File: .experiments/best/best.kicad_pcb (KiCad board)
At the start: 2 copper layers, 140 x 90 mm, 39 parts, among them J1 USB_C, J2 Output, J3 Debug, Q1 FS8205A, U1 USBLC6-2SC6, U2 BQ24072, U3 HY2113-KB5B, U4 MT3608, U5 AP2112K-3.3, U6 LN61CN3302MR-G

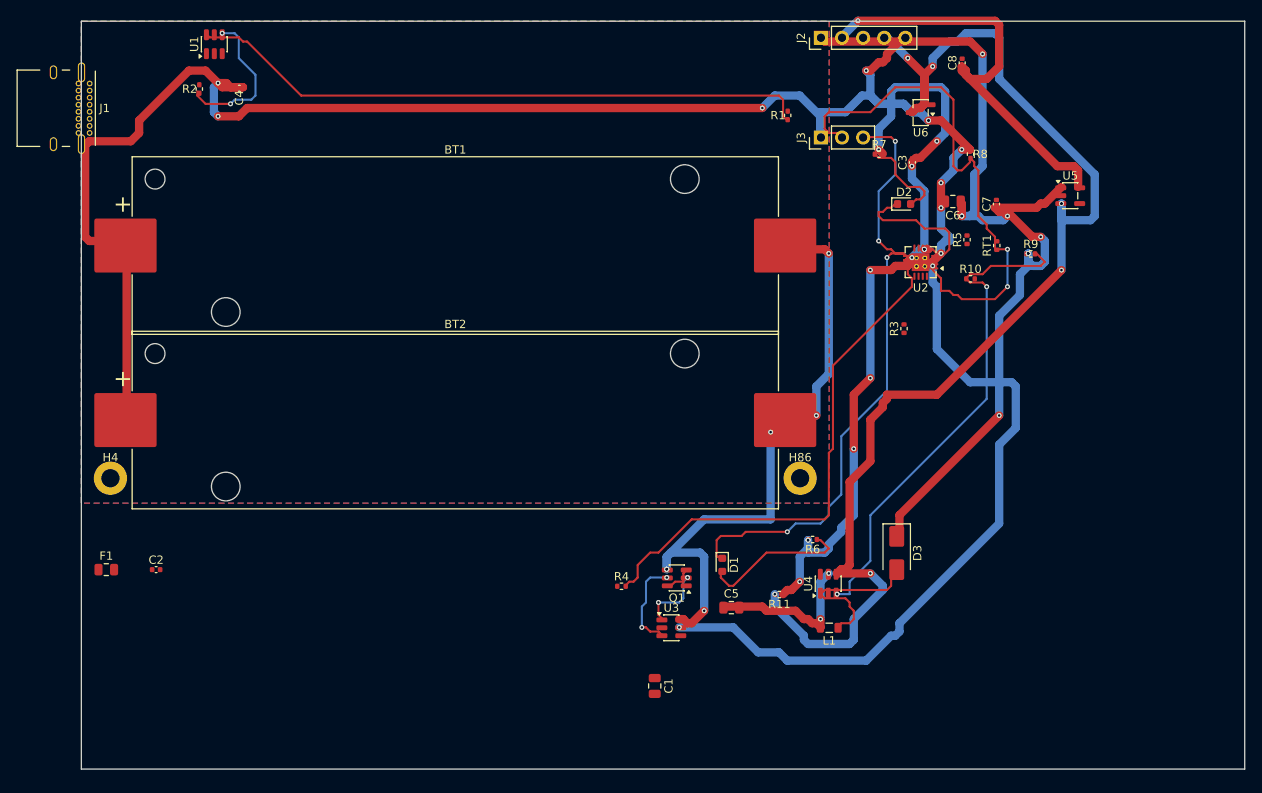
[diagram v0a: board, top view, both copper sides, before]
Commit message: 45-round experiment: best score 25.66, all nets routed (26/26)
Fixed A* performance by increasing max_search from 100k->500k to handle
high trace costs (100.0) without timing out. Kept high cost + coarse grid
(0.5mm) to prevent shorts while still routing efficiently.

Best config: edge_margin=5.7493mm, cooling_factor=0.9764, existing_trace_cost=200, max_rips=8

Co-Authored-By: Claude Opus 4.6 <noreply@anthropic.com>
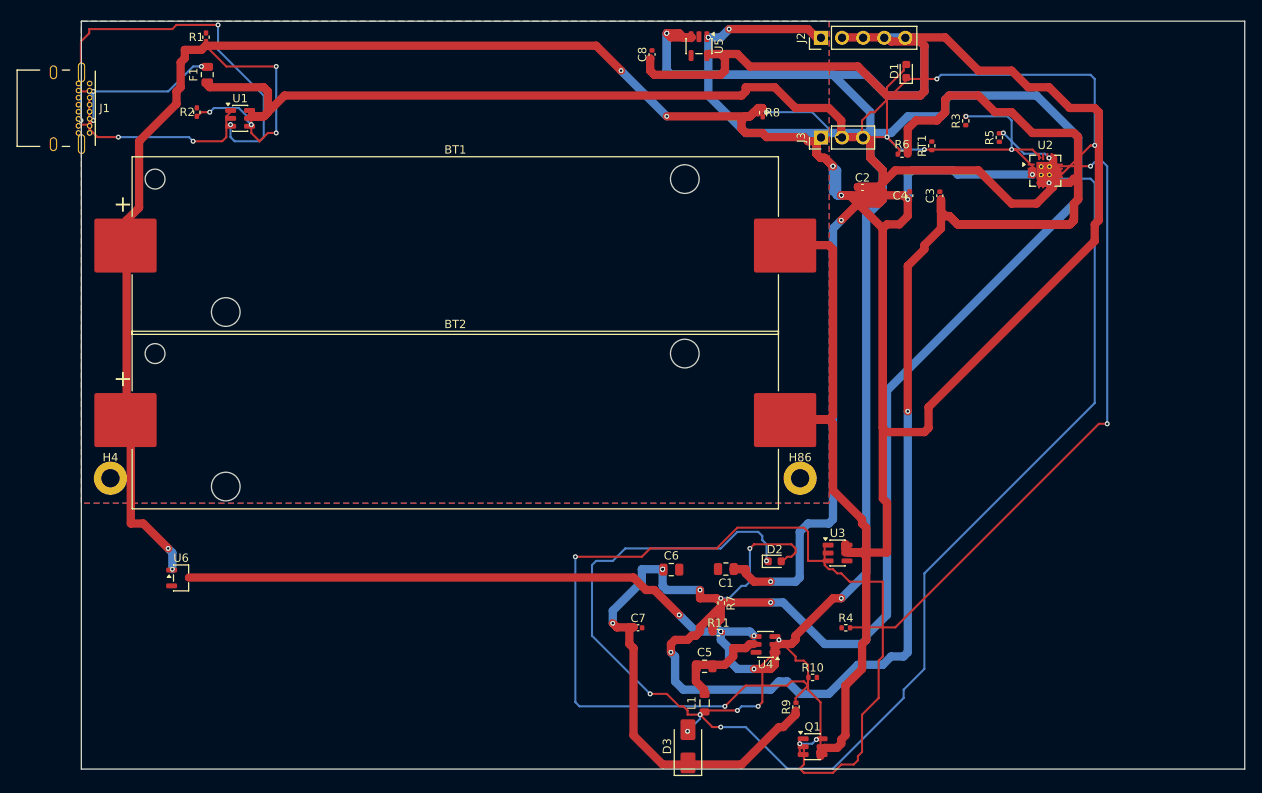
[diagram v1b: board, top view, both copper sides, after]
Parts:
- moved U6 105.2 mm to (12.0, 67.0), turned to 0 degrees
- moved C2 96.6 mm to (94.0, 20.0)
- moved C4 81.7 mm to (99.7, 21.0), turned to 90 degrees
- moved R1 70.6 mm to (15.0, 1.92)
- moved C7 66.8 mm to (67.0, 73.0), turned to 0 degrees
- moved D1 63.4 mm to (99.3, 6.00), turned to 90 degrees
- moved R9 61.4 mm to (86.0, 82.5), turned to 90 degrees
- moved F1 60.8 mm to (15.2, 6.43), turned to 90 degrees
- moved R7 57.3 mm to (77.0, 70.0), turned to -90 degrees
- moved C6 55.8 mm to (71.0, 66.0), turned to 0 degrees
- moved R10 51.6 mm to (88.0, 79.0)
- moved U5 48.2 mm to (74.3, 3.00), turned to -90 degrees
- moved R6 47.6 mm to (98.8, 16.0), turned to 0 degrees
- moved D2 45.7 mm to (83.4, 65.0)
- moved C8 37.3 mm to (68.7, 4.00)
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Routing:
- net /VBUS: track 0.00 -> 197.8 mm, vias 0 -> 2
- net Net-(D2-K): track 18.7 -> 159.5 mm, vias 0 -> 4
- net /5V: track 115.5 -> 224.6 mm, vias 8 -> 9
- net /VSYS: track 93.0 -> 191.5 mm, vias 12 -> 2
- net /EN: track 149.0 -> 240.3 mm, vias 8 -> 10
- net Net-(Q1B-G): track 11.3 -> 90.9 mm
- net /VBAT: track 293.0 -> 362.0 mm, vias 14 -> 10
- net Net-(R1-Pad1): track 75.5 -> 24.4 mm, vias 0 -> 2
- net Net-(U4-FB): track 60.0 -> 10.9 mm, vias 2 -> 0
- net Net-(J1-CC2): track 0.00 -> 48.8 mm, vias 0 -> 4
- net Net-(Q1A-G): track 8.12 -> 44.1 mm, vias 2 -> 0
- net /CHG_N: track 75.4 -> 46.6 mm, vias 4 -> 2
- net /NTC_SENSE: track 62.8 -> 35.4 mm, vias 2 -> 4
- net Net-(J1-CC1): track 0.00 -> 24.5 mm, vias 0 -> 2
- net Net-(F1-Pad2): track 0.00 -> 21.7 mm, vias 0 -> 4
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
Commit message: Run 75-round experiment with 5mil traces: score 29.0
Configured all traces (signal and power) to 5 mil (0.127mm).
Best layout: 26/26 nets routed, 531 traces, 92 vias, 2487mm total length.
DRC: 242 violations (improved from 339 baseline).

Best config: clearance=0.1757mm, edge_margin=5.8486mm, cooling_factor=0.9698

Co-Authored-By: Claude Opus 4.6 <noreply@anthropic.com>
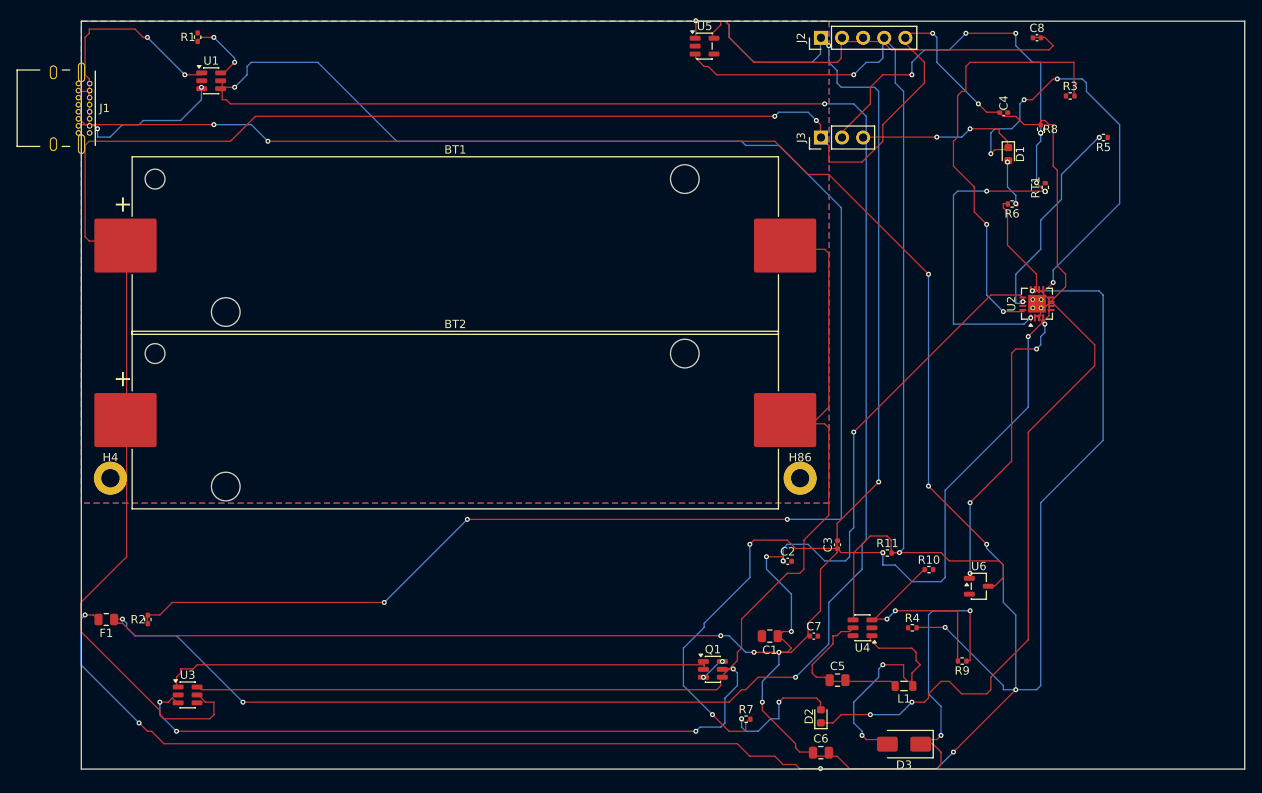
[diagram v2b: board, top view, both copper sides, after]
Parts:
- moved U6 96.0 mm to (108.0, 68.0)
- moved U3 80.1 mm to (12.8, 81.1)
- moved F1 66.7 mm to (3.00, 72.0), turned to 180 degrees
- moved R2 61.3 mm to (8.00, 72.0)
- moved C8 46.4 mm to (115.0, 2.00), turned to 0 degrees
- moved C2 45.9 mm to (85.0, 65.0)
- moved C3 43.8 mm to (91.0, 63.0)
- moved R8 33.5 mm to (115.4, 13.0)
- moved C6 28.4 mm to (89.0, 88.0)
- moved D3 26.0 mm to (99.0, 87.0), turned to 180 degrees
- moved L1 24.1 mm to (99.0, 80.0), turned to 180 degrees
- moved R11 22.5 mm to (97.0, 64.0)
- moved C7 21.2 mm to (88.2, 74.0)
- moved R9 20.7 mm to (106.0, 77.0), turned to 180 degrees
- moved D2 19.5 mm to (89.0, 83.6), turned to 90 degrees
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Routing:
- net Net-(F1-Pad2): track 21.7 -> 298.3 mm, vias 4 -> 10
- net Net-(R2-Pad1): track 8.04 -> 210.3 mm, vias 2 -> 4
- net /VBUS: track 197.8 -> 393.0 mm, vias 2 -> 10
- net /EN: track 240.3 -> 124.8 mm, vias 10 -> 4
- net Net-(D2-K): track 159.5 -> 77.9 mm, vias 4 -> 2
- net /VSYS: track 191.5 -> 111.9 mm, vias 2 -> 4
- net /VBAT: track 362.0 -> 296.8 mm, vias 10 -> 8
- net /NTC_SENSE: track 35.4 -> 86.6 mm, vias 4 -> 10
- net /5V: track 224.6 -> 174.3 mm, vias 9 -> 8
- net /CELL_NEG: track 89.3 -> 137.1 mm
- net Net-(U2-ISET): track 13.1 -> 52.6 mm
- net Net-(J1-CC2): track 48.8 -> 19.3 mm, vias 4 -> 2
- net /CHG_N: track 46.6 -> 70.5 mm, vias 2 -> 6
- net Net-(Q1A-G): track 44.1 -> 65.9 mm
- net Net-(U2-TMR): track 7.24 -> 25.1 mm
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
